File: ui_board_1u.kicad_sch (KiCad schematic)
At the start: 39 parts, among them J1 X9555WV-2x06-6TV01, U1 AFC01-S30FCA-00, U2 SPX3819M5-L, U3 TPS61040DBV

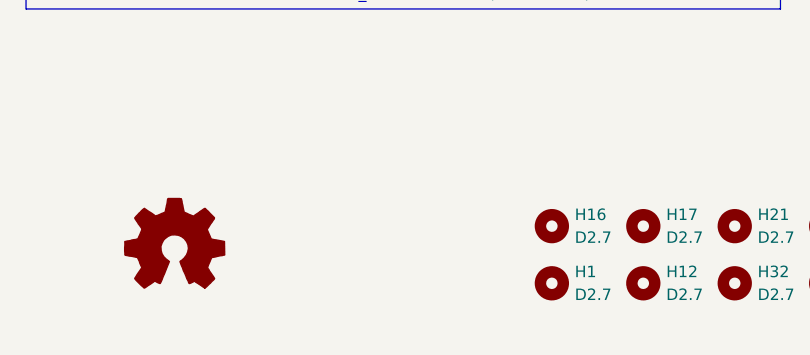
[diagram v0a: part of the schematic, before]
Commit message: rev1, port to kicad 10
  * revise LED resistor values. They were much to bright.
  * Change debouncing filter cap. from 10 nF to 100 nF
  * change to kicad 10
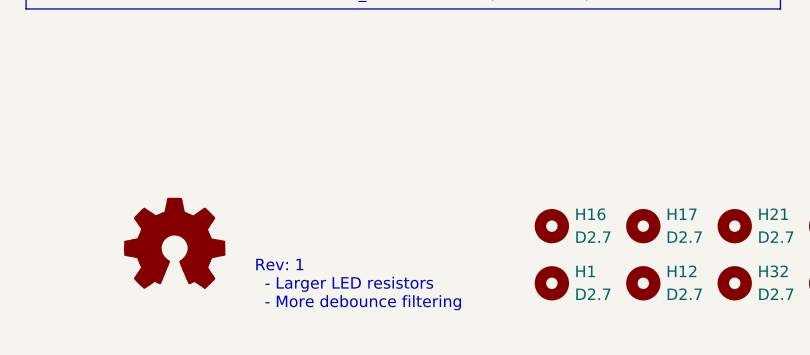
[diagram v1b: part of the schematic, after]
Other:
- note added: "Rev: 1 - Larger LED resistors - More debounce filtering"
